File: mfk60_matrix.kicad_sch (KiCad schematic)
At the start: 122 parts, among them SW2 COL1_ROW1, SW2 COL1_ROW2, SW2 COL1_ROW3, SW2 COL1_ROW4, SW2 COL1_ROW5, SW2 COL7_ROW1, SW2 COL7_ROW2, SW2 COL7_ROW3, SW2 COL7_ROW4, SW2 COL7_ROW5, SW3 COL10_ROW1, SW3 COL10_ROW2, SW3 COL10_ROW3, SW3 COL10_ROW4, SW3 COL10_ROW5, SW3 COL11_ROW1, SW3 COL11_ROW2, SW3 COL11_ROW3, SW3 COL11_ROW4, SW3 COL12_ROW1, SW3 COL12_ROW2, SW3 COL12_ROW3, SW3 COL12_ROW4, SW3 COL13_ROW1, SW3 COL13_ROW2, SW3 COL13_ROW3, SW3 COL13_ROW4, SW3 COL14_ROW1, SW3 COL14_ROW2, SW3 COL2_ROW1, SW3 COL2_ROW2, SW3 COL2_ROW3, SW3 COL2_ROW4, SW3 COL2_ROW5, SW3 COL3_ROW1, SW3 COL3_ROW2, SW3 COL3_ROW3, SW3 COL3_ROW4, SW3 COL3_ROW5, SW3 COL4_ROW1, SW3 COL4_ROW2, SW3 COL4_ROW3, SW3 COL4_ROW4, SW3 COL5_ROW1, SW3 COL5_ROW2, SW3 COL5_ROW3, SW3 COL5_ROW4, SW3 COL6_ROW1, SW3 COL6_ROW2, SW3 COL6_ROW3, SW3 COL6_ROW4, SW3 COL8_ROW1, SW3 COL8_ROW2, SW3 COL8_ROW3, SW3 COL8_ROW4, SW3 COL8_ROW5, SW3 COL9_ROW1, SW3 COL9_ROW2, SW3 COL9_ROW3, SW3 COL9_ROW4, SW3 COL9_ROW5

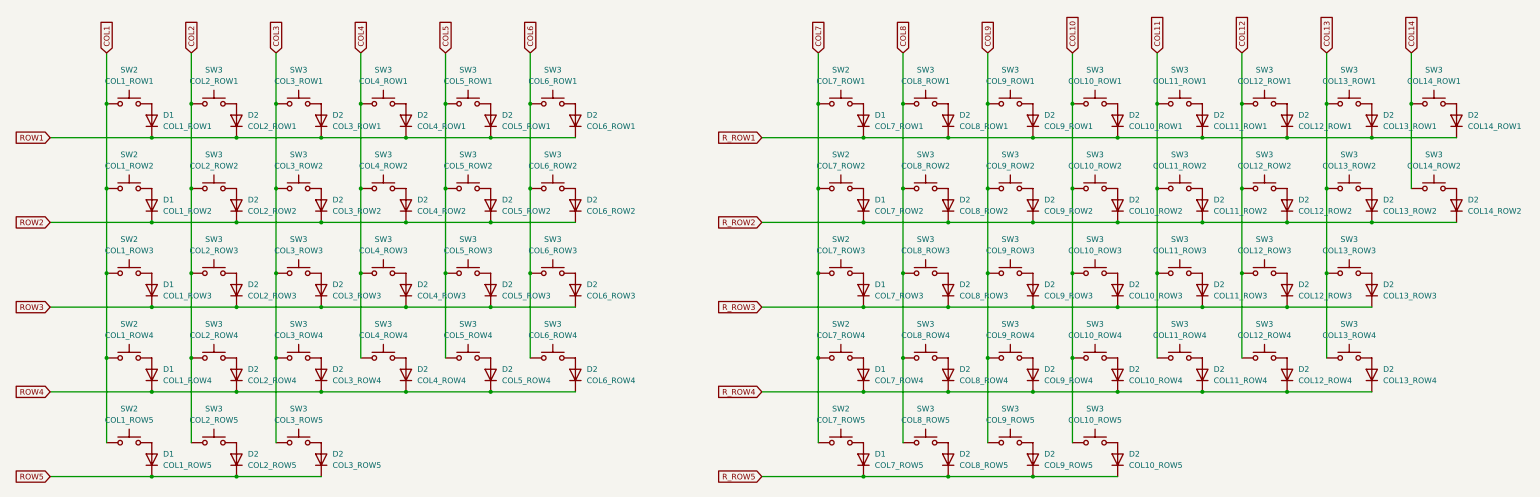
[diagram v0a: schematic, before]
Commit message: FIX: key and diode value
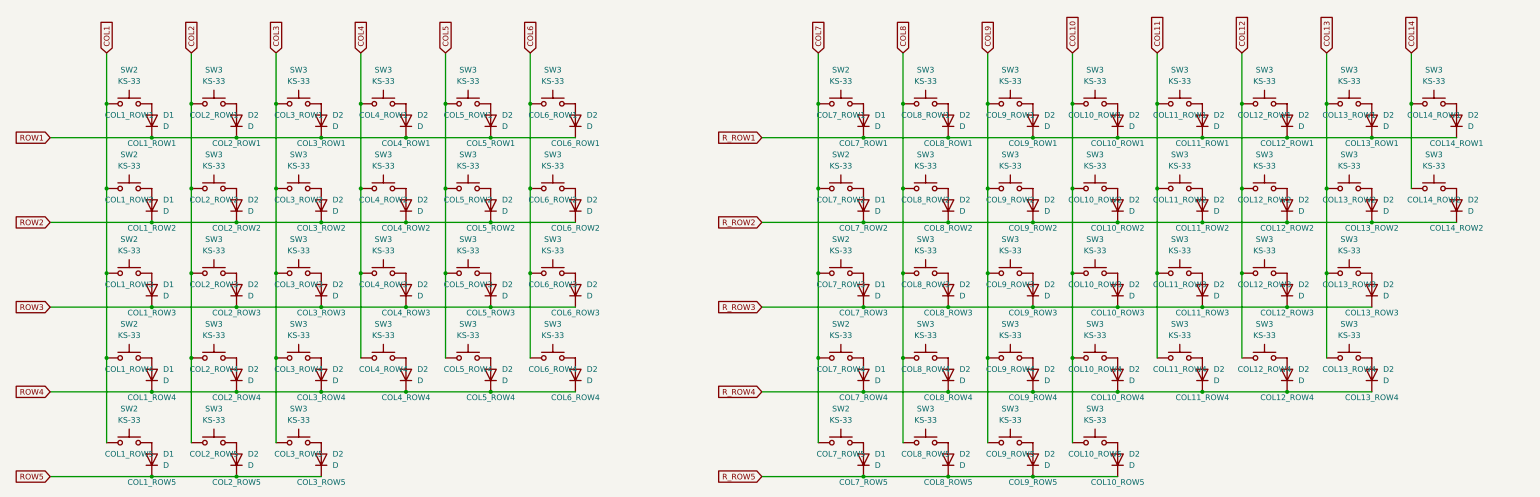
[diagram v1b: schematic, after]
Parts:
- D1: value COL7_ROW2 -> D; LCSC (none) -> C81598; Matrix (none) -> COL7_ROW2
- D1: value COL1_ROW5 -> D; LCSC (none) -> C81598; Matrix (none) -> COL1_ROW5
- D1: value COL7_ROW5 -> D; LCSC (none) -> C81598; Matrix (none) -> COL7_ROW5
- D1: value COL7_ROW1 -> D; LCSC (none) -> C81598; Matrix (none) -> COL7_ROW1
- D1: value COL1_ROW4 -> D; LCSC (none) -> C81598; Matrix (none) -> COL1_ROW4
- D1: value COL7_ROW3 -> D; LCSC (none) -> C81598; Matrix (none) -> COL7_ROW3
- D1: value COL1_ROW2 -> D; LCSC (none) -> C81598; Matrix (none) -> COL1_ROW2
- D1: value COL7_ROW4 -> D; LCSC (none) -> C81598; Matrix (none) -> COL7_ROW4
- D1: value COL1_ROW1 -> D; LCSC (none) -> C81598; Matrix (none) -> COL1_ROW1
- D1: value COL1_ROW3 -> D; LCSC (none) -> C81598; Matrix (none) -> COL1_ROW3
- D2: value COL8_ROW5 -> D; LCSC (none) -> C81598; Matrix (none) -> COL8_ROW5
- D2: value COL13_ROW3 -> D; LCSC (none) -> C81598; Matrix (none) -> COL13_ROW3
- D2: value COL2_ROW3 -> D; LCSC (none) -> C81598; Matrix (none) -> COL2_ROW3
- D2: value COL14_ROW1 -> D; LCSC (none) -> C81598; Matrix (none) -> COL14_ROW1
- D2: value COL12_ROW2 -> D; LCSC (none) -> C81598; Matrix (none) -> COL12_ROW2
- D2: value COL10_ROW3 -> D; LCSC (none) -> C81598; Matrix (none) -> COL10_ROW3
- D2: value COL6_ROW3 -> D; LCSC (none) -> C81598; Matrix (none) -> COL6_ROW3
- D2: value COL3_ROW4 -> D; LCSC (none) -> C81598; Matrix (none) -> COL3_ROW4
- D2: value COL9_ROW5 -> D; LCSC (none) -> C81598; Matrix (none) -> COL9_ROW5
- D2: value COL3_ROW1 -> D; LCSC (none) -> C81598; Matrix (none) -> COL3_ROW1
- D2: value COL6_ROW2 -> D; LCSC (none) -> C81598; Matrix (none) -> COL6_ROW2
- D2: value COL3_ROW2 -> D; LCSC (none) -> C81598; Matrix (none) -> COL3_ROW2
- D2: value COL3_ROW5 -> D; LCSC (none) -> C81598; Matrix (none) -> COL3_ROW5
- D2: value COL9_ROW2 -> D; LCSC (none) -> C81598; Matrix (none) -> COL9_ROW2
- D2: value COL13_ROW2 -> D; LCSC (none) -> C81598; Matrix (none) -> COL13_ROW2
- D2: value COL8_ROW3 -> D; LCSC (none) -> C81598; Matrix (none) -> COL8_ROW3
- D2: value COL12_ROW3 -> D; LCSC (none) -> C81598; Matrix (none) -> COL12_ROW3
- D2: value COL12_ROW1 -> D; LCSC (none) -> C81598; Matrix (none) -> COL12_ROW1
- D2: value COL2_ROW4 -> D; LCSC (none) -> C81598; Matrix (none) -> COL2_ROW4
- D2: value COL2_ROW1 -> D; LCSC (none) -> C81598; Matrix (none) -> COL2_ROW1
- D2: value COL6_ROW1 -> D; LCSC (none) -> C81598; Matrix (none) -> COL6_ROW1
- D2: value COL11_ROW2 -> D; LCSC (none) -> C81598; Matrix (none) -> COL11_ROW2
- D2: value COL8_ROW1 -> D; LCSC (none) -> C81598; Matrix (none) -> COL8_ROW1
- D2: value COL9_ROW1 -> D; LCSC (none) -> C81598; Matrix (none) -> COL9_ROW1
- D2: value COL6_ROW4 -> D; LCSC (none) -> C81598; Matrix (none) -> COL6_ROW4
- D2: value COL3_ROW3 -> D; LCSC (none) -> C81598; Matrix (none) -> COL3_ROW3
- D2: value COL5_ROW4 -> D; LCSC (none) -> C81598; Matrix (none) -> COL5_ROW4
- D2: value COL13_ROW1 -> D; LCSC (none) -> C81598; Matrix (none) -> COL13_ROW1
- D2: value COL10_ROW5 -> D; LCSC (none) -> C81598; Matrix (none) -> COL10_ROW5
- D2: value COL10_ROW1 -> D; LCSC (none) -> C81598; Matrix (none) -> COL10_ROW1
- D2: value COL11_ROW3 -> D; LCSC (none) -> C81598; Matrix (none) -> COL11_ROW3
- D2: value COL5_ROW3 -> D; LCSC (none) -> C81598; Matrix (none) -> COL5_ROW3
- D2: value COL5_ROW2 -> D; LCSC (none) -> C81598; Matrix (none) -> COL5_ROW2
- D2: value COL4_ROW4 -> D; LCSC (none) -> C81598; Matrix (none) -> COL4_ROW4
- D2: value COL10_ROW4 -> D; LCSC (none) -> C81598; Matrix (none) -> COL10_ROW4
- D2: value COL14_ROW2 -> D; LCSC (none) -> C81598; Matrix (none) -> COL14_ROW2
- D2: value COL4_ROW1 -> D; LCSC (none) -> C81598; Matrix (none) -> COL4_ROW1
- D2: value COL4_ROW2 -> D; LCSC (none) -> C81598; Matrix (none) -> COL4_ROW2
- D2: value COL12_ROW4 -> D; LCSC (none) -> C81598; Matrix (none) -> COL12_ROW4
- D2: value COL8_ROW4 -> D; LCSC (none) -> C81598; Matrix (none) -> COL8_ROW4
- D2: value COL9_ROW4 -> D; LCSC (none) -> C81598; Matrix (none) -> COL9_ROW4
- D2: value COL4_ROW3 -> D; LCSC (none) -> C81598; Matrix (none) -> COL4_ROW3
- D2: value COL9_ROW3 -> D; LCSC (none) -> C81598; Matrix (none) -> COL9_ROW3
- D2: value COL5_ROW1 -> D; LCSC (none) -> C81598; Matrix (none) -> COL5_ROW1
- D2: value COL11_ROW4 -> D; LCSC (none) -> C81598; Matrix (none) -> COL11_ROW4
- D2: value COL10_ROW2 -> D; LCSC (none) -> C81598; Matrix (none) -> COL10_ROW2
- D2: value COL8_ROW2 -> D; LCSC (none) -> C81598; Matrix (none) -> COL8_ROW2
- D2: value COL2_ROW5 -> D; LCSC (none) -> C81598; Matrix (none) -> COL2_ROW5
- D2: value COL13_ROW4 -> D; LCSC (none) -> C81598; Matrix (none) -> COL13_ROW4
- D2: value COL11_ROW1 -> D; LCSC (none) -> C81598; Matrix (none) -> COL11_ROW1
- D2: value COL2_ROW2 -> D; LCSC (none) -> C81598; Matrix (none) -> COL2_ROW2
- SW2: value COL7_ROW5 -> KS-33; Matrix (none) -> COL7_ROW5
- SW2: value COL7_ROW3 -> KS-33; Matrix (none) -> COL7_ROW3
- SW2: value COL1_ROW4 -> KS-33; Matrix (none) -> COL1_ROW4
- SW2: value COL7_ROW2 -> KS-33; Matrix (none) -> COL7_ROW2
- SW2: value COL1_ROW1 -> KS-33; Matrix (none) -> COL1_ROW1
- SW2: value COL7_ROW1 -> KS-33; Matrix (none) -> COL7_ROW1
- SW2: value COL1_ROW3 -> KS-33; Matrix (none) -> COL1_ROW3
- SW2: value COL1_ROW2 -> KS-33; Matrix (none) -> COL1_ROW2
- SW2: value COL7_ROW4 -> KS-33; Matrix (none) -> COL7_ROW4
- SW2: value COL1_ROW5 -> KS-33; Matrix (none) -> COL1_ROW5
- SW3: value COL4_ROW1 -> KS-33; Matrix (none) -> COL4_ROW1
- SW3: value COL5_ROW2 -> KS-33; Matrix (none) -> COL5_ROW2
- SW3: value COL3_ROW2 -> KS-33; Matrix (none) -> COL3_ROW2
- SW3: value COL2_ROW1 -> KS-33; Matrix (none) -> COL2_ROW1
- SW3: value COL6_ROW2 -> KS-33; Matrix (none) -> COL6_ROW2
- SW3: value COL13_ROW2 -> KS-33; Matrix (none) -> COL13_ROW2
- SW3: value COL10_ROW4 -> KS-33; Matrix (none) -> COL10_ROW4
- SW3: value COL10_ROW2 -> KS-33; Matrix (none) -> COL10_ROW2
- SW3: value COL8_ROW4 -> KS-33; Matrix (none) -> COL8_ROW4
- SW3: value COL8_ROW1 -> KS-33; Matrix (none) -> COL8_ROW1
- SW3: value COL13_ROW1 -> KS-33; Matrix (none) -> COL13_ROW1
- SW3: value COL5_ROW3 -> KS-33; Matrix (none) -> COL5_ROW3
- SW3: value COL2_ROW3 -> KS-33; Matrix (none) -> COL2_ROW3
- SW3: value COL4_ROW2 -> KS-33; Matrix (none) -> COL4_ROW2
- SW3: value COL12_ROW4 -> KS-33; Matrix (none) -> COL12_ROW4
- SW3: value COL10_ROW1 -> KS-33; Matrix (none) -> COL10_ROW1
- SW3: value COL2_ROW2 -> KS-33; Matrix (none) -> COL2_ROW2
- SW3: value COL13_ROW3 -> KS-33; Matrix (none) -> COL13_ROW3
- SW3: value COL9_ROW3 -> KS-33; Matrix (none) -> COL9_ROW3
- SW3: value COL14_ROW2 -> KS-33; Matrix (none) -> COL14_ROW2
- SW3: value COL12_ROW2 -> KS-33; Matrix (none) -> COL12_ROW2
- SW3: value COL2_ROW5 -> KS-33; Matrix (none) -> COL2_ROW5
- SW3: value COL11_ROW3 -> KS-33; Matrix (none) -> COL11_ROW3
- SW3: value COL8_ROW2 -> KS-33; Matrix (none) -> COL8_ROW2
- SW3: value COL3_ROW1 -> KS-33; Matrix (none) -> COL3_ROW1
- SW3: value COL6_ROW4 -> KS-33; Matrix (none) -> COL6_ROW4
- SW3: value COL12_ROW1 -> KS-33; Matrix (none) -> COL12_ROW1
- SW3: value COL5_ROW4 -> KS-33; Matrix (none) -> COL5_ROW4
- SW3: value COL5_ROW1 -> KS-33; Matrix (none) -> COL5_ROW1
- SW3: value COL13_ROW4 -> KS-33; Matrix (none) -> COL13_ROW4
- SW3: value COL12_ROW3 -> KS-33; Matrix (none) -> COL12_ROW3
- SW3: value COL4_ROW3 -> KS-33; Matrix (none) -> COL4_ROW3
- SW3: value COL9_ROW1 -> KS-33; Matrix (none) -> COL9_ROW1
- SW3: value COL10_ROW5 -> KS-33; Matrix (none) -> COL10_ROW5
- SW3: value COL9_ROW5 -> KS-33; Matrix (none) -> COL9_ROW5
- SW3: value COL11_ROW1 -> KS-33; Matrix (none) -> COL11_ROW1
- SW3: value COL10_ROW3 -> KS-33; Matrix (none) -> COL10_ROW3
- SW3: value COL3_ROW3 -> KS-33; Matrix (none) -> COL3_ROW3
- SW3: value COL14_ROW1 -> KS-33; Matrix (none) -> COL14_ROW1
- SW3: value COL9_ROW4 -> KS-33; Matrix (none) -> COL9_ROW4
- SW3: value COL9_ROW2 -> KS-33; Matrix (none) -> COL9_ROW2
- SW3: value COL4_ROW4 -> KS-33; Matrix (none) -> COL4_ROW4
- SW3: value COL2_ROW4 -> KS-33; Matrix (none) -> COL2_ROW4
- SW3: value COL8_ROW5 -> KS-33; Matrix (none) -> COL8_ROW5
- SW3: value COL8_ROW3 -> KS-33; Matrix (none) -> COL8_ROW3
- SW3: value COL6_ROW1 -> KS-33; Matrix (none) -> COL6_ROW1
- SW3: value COL3_ROW4 -> KS-33; Matrix (none) -> COL3_ROW4
- SW3: value COL11_ROW4 -> KS-33; Matrix (none) -> COL11_ROW4
- SW3: value COL6_ROW3 -> KS-33; Matrix (none) -> COL6_ROW3
- SW3: value COL11_ROW2 -> KS-33; Matrix (none) -> COL11_ROW2
- SW3: value COL3_ROW5 -> KS-33; Matrix (none) -> COL3_ROW5
